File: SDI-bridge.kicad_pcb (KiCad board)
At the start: 4 copper layers, 68 x 32.6 mm, 168 parts, among them J1 031-70526-21, J2 WE_68715014522, J3 031-70526-21, J4 MC-HVT1-S04-G, J5 MC-HVT1-S04-G, U1 GS2971A, U2 MAX8902B, U3 GS2988, U4 CrossLink_LIF-MD6000-6JMG80I, U5 SC18IS602BIPW, Y1 ABM7_27.000MH_D2Y_T

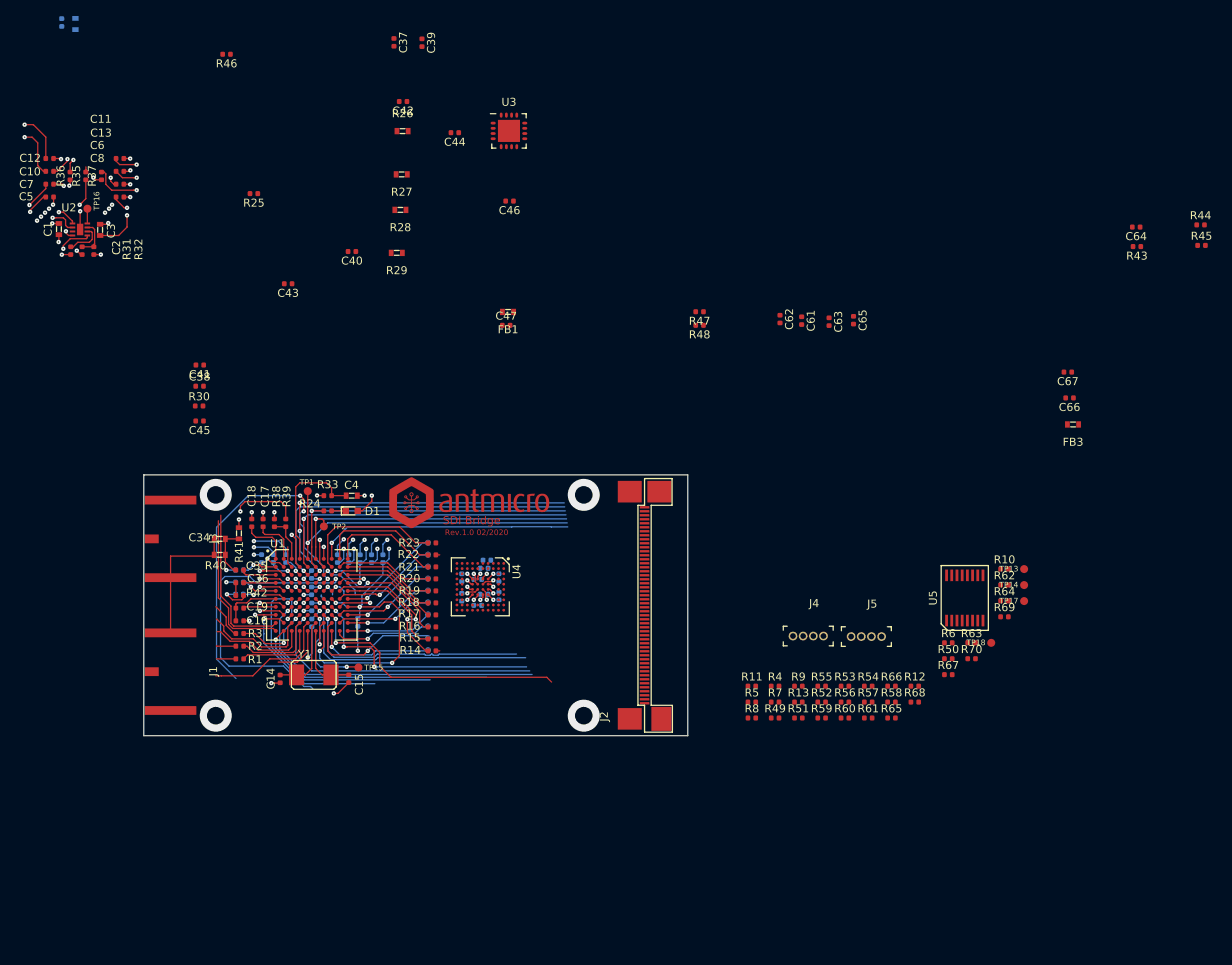
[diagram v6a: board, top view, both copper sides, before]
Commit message: Update component placement
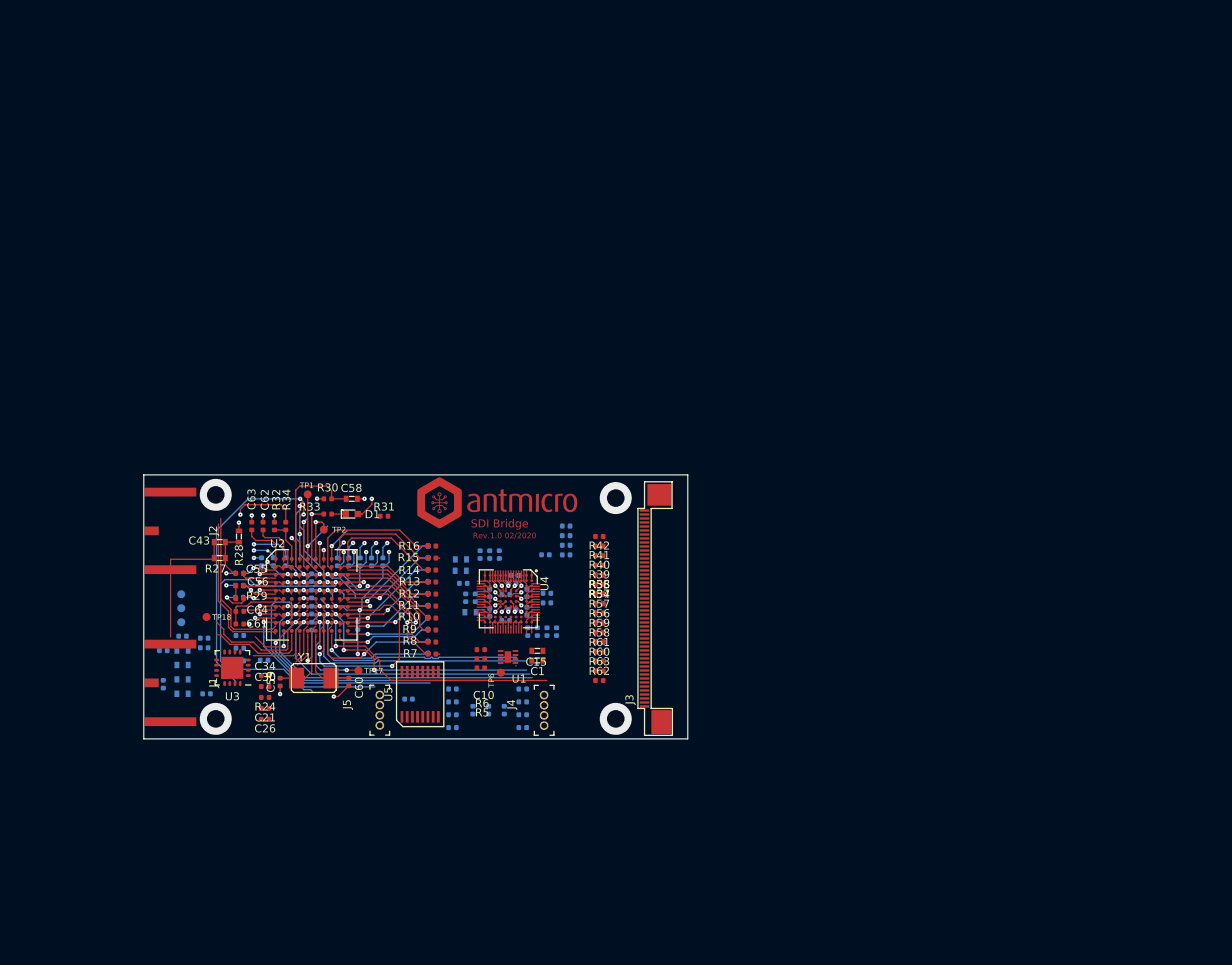
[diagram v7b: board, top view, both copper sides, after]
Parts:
- removed the C11 at (97.0, 60.5)
- removed the C12 at (88.2, 60.5)
- removed the C13 at (97.0, 62.1)
- removed the C2 at (90.9, 72.0)
- removed the C3 at (94.5, 69.4)
- removed the C38 at (107.0, 88.9)
- removed the C42 at (132.4, 53.3)
- removed the C43 at (118.0, 76.1)
- removed the C45 at (107.0, 93.3)
- removed the C48 at (139.8, 115.3)
- removed the C5 at (88.2, 65.3)
- removed the C51 at (141.7, 116.3)
- removed the C52 at (142.6, 111.7)
- removed the C58 at (142.9, 110.7)
- removed the C59 at (142.5, 114.9)
- removed the C6 at (97.0, 63.7)
- removed the C60 at (144.4, 115.1)
- removed the C61 at (182.2, 80.7)
- removed the C7 at (88.2, 63.7)
- removed the C8 at (97.0, 65.3)
- removed the J2 at (162.0, 116.3)
- removed the R10 at (207.6, 111.8)
- removed the R11 at (176.0, 126.4)
- removed the R12 at (196.4, 126.4)
- removed the R13 at (181.8, 128.4)
- removed the R30 at (106.9, 91.4)
- removed the R32 at (93.8, 72.0)
- removed the R35 at (92.8, 62.6)
- removed the R36 at (90.8, 62.6)
- removed the R4 at (178.9, 126.4)
- removed the R64 at (207.6, 115.8)
- removed the R68 at (196.4, 128.4)
- removed R69, R70: R_0R_0402, antmicro-footprints:0402-res
- removed the R8 at (176.0, 130.4)
- removed the R9 at (181.8, 126.4)
- removed the TP16 at (93.0, 66.7)
- removed the U2 at (92.0, 69.3)
- added C15: C_10u_0603, antmicro-footprints:0603-cap, F.Cu at (149.2, 122.0)
- added C19: C_10n_0402, antmicro-footprints:0402-cap, B.Cu at (138.6, 126.8)
- added C20: C_10n_0402, antmicro-footprints:0402-cap, B.Cu at (147.4, 128.4)
- added C21: C_10n_0402, antmicro-footprints:0402-cap, F.Cu at (115.2, 129.2)
- added C24: C_1u_0402, antmicro-footprints:0402-cap, B.Cu at (138.6, 128.4)
- added C25: C_1u_0402, antmicro-footprints:0402-cap, B.Cu at (147.4, 126.8)
- added C26: C_1u_0402, antmicro-footprints:0402-cap, F.Cu at (115.2, 130.6)
- added C27: C_5n6_0402, antmicro-footprints:0402-res, B.Cu at (104.8, 120.2)
- added C28: C_1u_0402, antmicro-footprints:0402-cap, B.Cu at (138.6, 130.0)
- added C29: C_1u_0402, antmicro-footprints:0402-cap, B.Cu at (147.4, 131.6)
- added C30: C_1u_0402, antmicro-footprints:0402-cap, F.Cu at (115.2, 126.5)
- added C32: C_10n_0402, antmicro-footprints:0402-cap, B.Cu at (138.6, 131.6)
- added C33: C_10n_0402, antmicro-footprints:0402-cap, B.Cu at (147.4, 130.0)
- added C34: C_10n_0402, antmicro-footprints:0402-cap, F.Cu at (115.2, 125.1)
- added C36: C_10n_0402, antmicro-footprints:0402-cap, B.Cu at (102.4, 126.2)
- added C39: C_100n_0402_6V3, antmicro-footprints:0402-cap, B.Cu at (148.0, 119.6)
- added C40: C_100n_0402_6V3, antmicro-footprints:0402-cap, B.Cu at (147.9, 114.8)
- added C44: C_100n_0402_6V3, antmicro-footprints:0402-cap, B.Cu at (146.4, 112.6)
- added C53: C_100n_0402_6V3, antmicro-footprints:0402-cap, B.Cu at (147.9, 117.0)
- added C54: C_100n_0402_6V3, antmicro-footprints:0402-cap, B.Cu at (145.2, 118.2)
- added J3: WE_68715014522_ONE-SIDE, antmicro-footprints:WE_68715014522_ONE-SIDE, F.Cu at (162.0, 116.7)
- added R21: R_0R_0402, antmicro-footprints:0402-res, B.Cu at (143.1, 129.4)
- added R22: R_0R_0402, antmicro-footprints:0402-res, B.Cu at (141.1, 129.4)
- added R23: R_0R_0402, antmicro-footprints:0402-res, B.Cu at (145.1, 129.4)
- added R24: R_0R_0402, antmicro-footprints:0402-res, F.Cu at (115.2, 127.8)
- added R38: R_0R_0402, antmicro-footprints:0402-res, F.Cu at (156.9, 112.5)
- added R39: R_0R_0402, antmicro-footprints:0402-res, F.Cu at (156.9, 111.3)
- added R40: R_0R_0402, antmicro-footprints:0402-res, F.Cu at (156.9, 110.1)
- added R41: R_0R_0402, antmicro-footprints:0402-res, F.Cu at (156.9, 108.9)
- added R42: R_0R_0402, antmicro-footprints:0402-res, F.Cu at (156.9, 107.7)
- added R44: R_0R_0402, antmicro-footprints:0402-res, B.Cu at (156.9, 113.7)
- added R45: R_0R_0402, antmicro-footprints:0402-res, B.Cu at (156.9, 112.5)
- added R6: R_120k_0402, antmicro-footprints:0402-res, F.Cu at (142.1, 123.0)
- added R66: R_2k37_0402, antmicro-footprints:0402-res, B.Cu at (152.8, 108.8)
- added TP6: TP_SMD1MM, antmicro-footprints:Testpoint_smd_1mm, F.Cu at (144.6, 124.7)
- added U1: MAX8902B, antmicro-footprints:TDFN2x2, F.Cu at (145.5, 122.8)
- C10: value C_1u_0402 -> C_10n_0402
- C18: renamed from C37; moved to B.Cu
- C22: renamed from C39; moved to B.Cu
- C23: renamed from C40; moved to B.Cu
- C31: renamed from C44; moved to B.Cu
- C37: renamed from C47; moved to B.Cu
- C41: value C_1u_0402 -> C_100n_0402_6V3; moved to B.Cu
- C42: renamed from C62; moved to B.Cu
- C45: renamed from C64; moved to B.Cu
- C46: value C_10n_0402 -> C_100n_0402_6V3; moved to B.Cu
- C47: renamed from C66; moved to B.Cu
- C48: renamed from C63; moved to B.Cu
- C51: renamed from C67; moved to B.Cu
- C52: renamed from C65; moved to B.Cu
- FB1, FB3, R1, R2, R3, R47, R49, R50, R51, R52, R53, R67: moved to B.Cu
- R17: renamed from R26; moved to B.Cu
- R18: renamed from R27; moved to B.Cu
- R19: renamed from R28; moved to B.Cu
- R20: renamed from R29; moved to B.Cu
- R26: renamed from R43; moved to B.Cu
- R31: value R_120k_0402 -> R_0R_0402
- R35: renamed from R44; moved to B.Cu
- R36: renamed from R45; moved to B.Cu
- R4: renamed from R25; moved to B.Cu
- R43: renamed from R6; moved to B.Cu
- R46, R48: value R_2k37_0402 -> R_0R_0402; moved to B.Cu
- R5: value R_2k37_0402 -> R_120k_0402
- R63: value R_2k37_0402 -> R_0R_0402
- R64: renamed from R7; moved to B.Cu
- R65: value R_0R_0402 -> R_2k37_0402; moved to B.Cu
- R68: renamed from R66; moved to B.Cu
- TP3: renamed from TP13; moved to B.Cu
- TP4: renamed from TP14; moved to B.Cu
- TP5: renamed from TP17; moved to B.Cu
- moved TP3 105.4 mm to (104.7, 115.0), turned to 180 degrees
- moved TP4 105.4 mm to (104.7, 116.7), turned to 180 degrees
- moved TP5 105.4 mm to (104.7, 118.5), turned to 180 degrees
- moved TP18 98.1 mm to (107.8, 117.7), turned to 180 degrees
- moved R36 97.0 mm to (143.2, 110.0), turned to 270 degrees
- moved R35 96.9 mm to (144.4, 110.0), turned to 270 degrees
- moved C45 86.7 mm to (150.4, 114.8)
- moved C38 86.2 mm to (139.9, 113.6), turned to 180 degrees
- moved R26 86.2 mm to (150.4, 116.0), turned to 0 degrees
- moved FB2 83.6 mm to (139.6, 112.0), turned to 0 degrees
- moved R46 83.0 mm to (156.9, 116.1)
- moved C1 80.5 mm to (149.2, 123.2), turned to 0 degrees
- moved R37 80.5 mm to (156.9, 113.7), turned to 180 degrees
- moved C10 80.5 mm to (142.1, 121.8)
- moved C47 79.5 mm to (140.2, 115.4), turned to 90 degrees
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- renumbered C28 to C11, C29 to C12, C30 to C13, C31 to C14, C32 to C16, C33 to C17, C20 to C2, C21 to C3, C9 to C35, C53 to C38, C22 to C4, C34 to C43, C23 to C5, C35 to C55, C36 to C56, C4 to C58, C14 to C59, C24 to C6, C15 to C60, C16 to C61, C17 to C62, C18 to C63, C19 to C64, C25 to C7, C26 to C8, C27 to C9, J3 to J2, R17 to R10, R18 to R11, R19 to R12, R20 to R13, R21 to R14, R22 to R15, R23 to R16, R34 to R25, R40 to R27, R41 to R28, R42 to R29, R33 to R30, R38 to R32, R24 to R33, R39 to R34, R14 to R7, R15 to R8, R16 to R9, TP6 to TP10, TP7 to TP11, TP8 to TP12, TP9 to TP13, TP10 to TP14, TP11 to TP15, TP12 to TP16, TP15 to TP17, TP3 to TP7, TP4 to TP8, TP5 to TP9, U1 to U2
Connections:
- net +VSW renamed IO_VDD
- net /VCO_VDD renamed VCO_VDD
- C10 pad 1: +3.3VA -> +1V2
- C10 pad 2: GNDA -> Net-(C10-Pad2)
- C18 pad 1: VDD -> CD_VDD
- C22 pad 1: VDD -> CD_VDD
- C38 pad 1: /VCCA_DPHY -> VCCA_DPHY
- C41 pad 1: +3V3 -> /VCCIO
- C46 pad 1: GNDA -> /VCCIO
- C46 pad 2: VDD -> GNDREF
- C49 pad 1: /VCCIO -> VCCA_DPHY
- C49 pad 2: GNDREF -> /GNDPLL_DPHY
- C57 pad 1: /VCCA_DPHY -> /VCCIO
- FB2 pad 2: /VCCA_DPHY -> VCCA_DPHY
- R31 pad 1: +1V2 -> /LOCKED
- R31 pad 2: Net-(R31-Pad2) -> /LOCKED_IN
- R35 pad 2: /VCCIO -> VCC_IO
- R36 pad 2: /VCCIO -> VCC_IO
- R37 pad 1: +1V2 -> /SDA1
- R37 pad 2: VPP -> /SDA_CL
- R46 pad 1: /SCL_GS -> /MIPI1_D0_N
- R46 pad 2: Net-(R4-Pad2) (its old number) -> /DPHY1_D0_N
- R47 pad 1: +3V3 -> /MIPI1_D0_P
- R47 pad 2: Net-(R4-Pad2) (its old number) -> /DPHY1_D0_P
- R48 pad 1: /SDA_GS -> /MIPI1_D1_N
- R48 pad 2: Net-(R4-Pad2) (its old number) -> /DPHY1_D1_N
- R49 pad 1: /DPHY0_D2_N -> /MIPI1_D1_P
- R49 pad 2: /MIPI0_D2_N -> /DPHY1_D1_P
- R5 pad 1: /SDA_CL -> +1V2
- R5 pad 2: Net-(R4-Pad2) (its old number) -> Net-(R5-Pad2)
- R50 pad 1: /DPHY0_D2_P -> /MIPI1_D2_N
- R50 pad 2: /MIPI0_D2_P -> /DPHY1_D2_N
- R51 pad 1: /DPHY0_D3_N -> /MIPI1_D2_P
- R51 pad 2: /MIPI0_D3_N -> /DPHY1_D2_P
- R52 pad 1: /DPHY0_D3_P -> /MIPI1_D3_N
- R52 pad 2: /MIPI0_D3_P -> /DPHY1_D3_N
- R53 pad 1: /DPHY1_CLK_N -> /MIPI1_D3_P
- R53 pad 2: /MIPI1_CLK_N -> /DPHY1_D3_P
- R54 pad 1: /DPHY1_CLK_P -> /DPHY0_CLK_N
- R54 pad 2: /MIPI1_CLK_P -> /MIPI0_CLK_N
- R55 pad 1: /DPHY1_D0_N -> /DPHY0_CLK_P
- R55 pad 2: /MIPI1_D0_N -> /MIPI0_CLK_P
- R56 pad 1: /DPHY1_D0_P -> /DPHY0_D0_N
- R56 pad 2: /MIPI1_D0_P -> /MIPI0_D0_N
- R57 pad 1: /DPHY1_D1_N -> /DPHY0_D0_P
- R57 pad 2: /MIPI1_D1_N -> /MIPI0_D0_P
- R58 pad 1: /DPHY1_D1_P -> /DPHY0_D1_N
- R58 pad 2: /MIPI1_D1_P -> /MIPI0_D1_N
- R59 pad 1: /DPHY1_D2_N -> /DPHY0_D1_P
- R59 pad 2: /MIPI1_D2_N -> /MIPI0_D1_P
- R60 pad 1: /DPHY1_D2_P -> /DPHY0_D2_N
- R60 pad 2: /MIPI1_D2_P -> /MIPI0_D2_N
- R61 pad 1: /DPHY1_D3_N -> /DPHY0_D2_P
- R61 pad 2: /MIPI1_D3_N -> /MIPI0_D2_P
- R62 pad 1: /DPHY1_D3_P -> /DPHY0_D3_N
- R62 pad 2: /MIPI1_D3_P -> /MIPI0_D3_N
- R63 pad 1: /SDA_CL -> /DPHY0_D3_P
- R63 pad 2: Net-(R63-Pad2) -> /MIPI0_D3_P
- R64 pad 1: /SCL_CL -> Net-(R64-Pad1)
- R64 pad 2: Net-(R63-Pad2) -> /SCL_CL
- R65 pad 1: +3V3 -> Net-(R64-Pad1)
- R65 pad 2: Net-(R63-Pad2) -> /SDA_CL
- R67 pad 1: /SDA_GS -> +3V3
- R67 pad 2: /SDA -> Net-(R64-Pad1)
- R68 pad 1: /SDA_GS -> Net-(R64-Pad1)
- R68 pad 2: Net-(R63-Pad2) -> /SDA_GS
- U3 pad 9: VDD -> CD_VDD
- U4 pad D1: Net-(U4-PadD1) -> /IOPROC_EN_~DIS~
- U4 pad D2: /VCCA_DPHY -> VCCA_DPHY
- U4 pad D4: /VCCA_DPHY -> VCCA_DPHY
- U4 pad D7: /VCCA_DPHY -> VCCA_DPHY
- U4 pad E2: /LOCKED -> /LOCKED_IN
- U4 pad E7: /VCCA_DPHY -> VCCA_DPHY
- U4 pad F4: /VCCIO -> VCC_IO
- U4 pad F5: /VCCIO -> VCC_IO
- U4 pad F6: /VCCIO -> VCC_IO
- U4 pad F7: /VCCIO -> VCC_IO
- U4 pad G4: /VCCIO -> VCC_IO
- U4 pad K2: Net-(U4-PadK2) -> /Audio_EN_~DIS~
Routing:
- net /Y_1ANC: track 42.4 -> 10.3 mm
- net /DATA_ERRORb: track 43.3 -> 11.6 mm
- net /LOCKED: track 40.4 -> 9.11 mm
- net /F_DE: track 39.2 -> 8.67 mm
- net /V_VSYNC: track 38.2 -> 8.96 mm
- net /H_HSYNC: track 41.9 -> 13.0 mm
- net /PCLK: track 32.3 -> 5.80 mm
- net +1V2: track 25.5 -> 9.68 mm, vias 13 -> 6
- net +3V3: track 16.9 -> 3.84 mm, vias 10 -> 2
- net +3.3VA: track 33.9 -> 21.2 mm, vias 7 -> 5
- net VPP: track 22.2 -> 10.1 mm, vias 7 -> 4
- net /AUDIO_OUTPUT_CH5_6: track 16.0 -> 5.12 mm
- net GNDREF: track 55.7 -> 46.5 mm, vias 36 -> 24
- net VCC_IO: track 0.00 -> 7.32 mm, vias 0 -> 5
- net GNDA: track 54.9 -> 48.1 mm, vias 30 -> 25
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- added copper zone on In1.Cu, net +VSW
- removed copper zone on In1.Cu, net IO_VDD
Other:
- board size 68 x 32.6 mm -> 68 x 33 mm

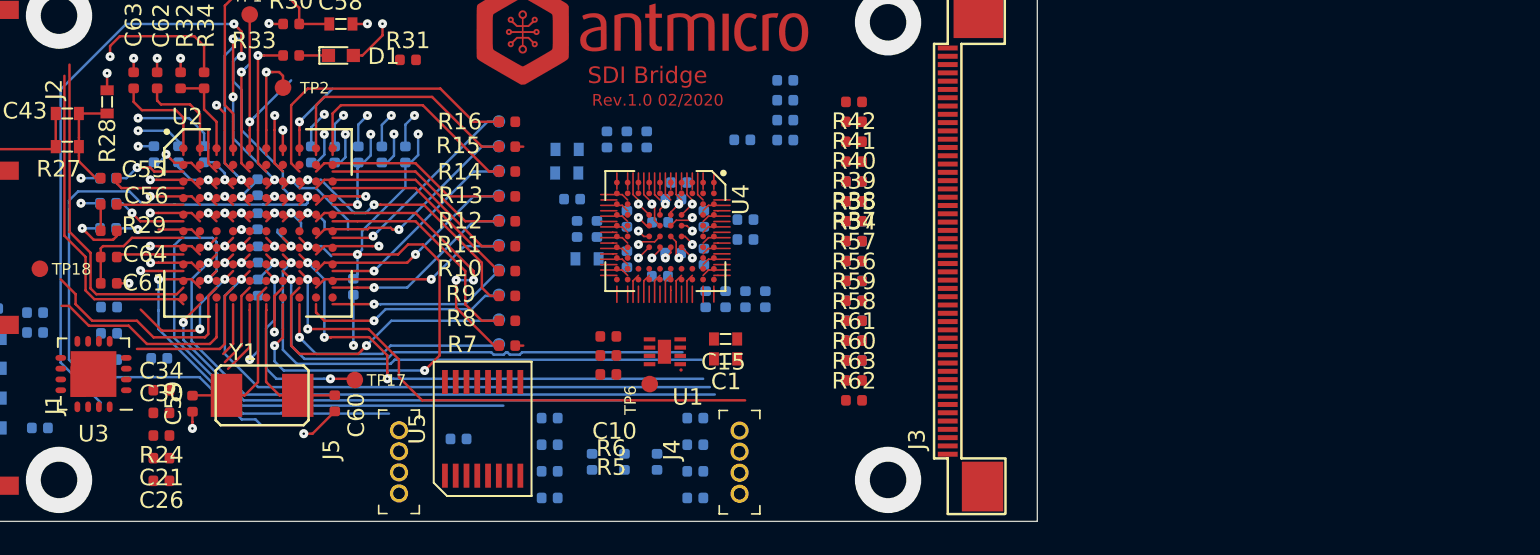
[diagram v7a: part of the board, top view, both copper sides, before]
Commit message: Schematic changes after design review
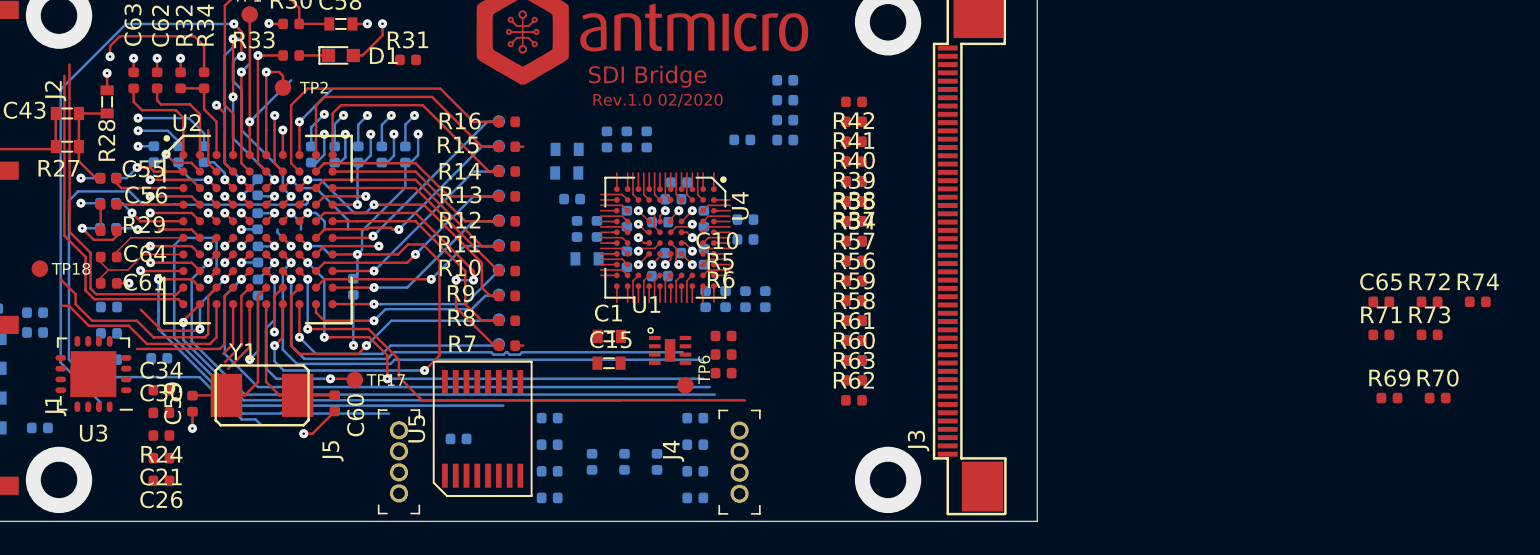
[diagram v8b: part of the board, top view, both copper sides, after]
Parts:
- added C65: C_10n_0402, antmicro-footprints:0402-cap, F.Cu at (188.8, 119.8)
- added R69: R_0R_0402, antmicro-footprints:0402-res, F.Cu at (189.2, 125.6)
- added R70: R_0R_0402, antmicro-footprints:0402-res, F.Cu at (192.2, 125.6)
- added R71: R_0R_0402, antmicro-footprints:0402-res, F.Cu at (188.8, 121.8)
- added R72: R_0R_0402, antmicro-footprints:0402-res, F.Cu at (191.7, 119.8)
- added R73: R_0R_0402, antmicro-footprints:0402-res, F.Cu at (191.7, 121.8)
- added R74: R_0R_0402, antmicro-footprints:0402-res, F.Cu at (194.6, 119.8)
- moved C15 7.18 mm to (142.2, 123.5), turned to 180 degrees
- moved C1 7.14 mm to (142.2, 121.8), turned to 180 degrees
- moved R5 7.05 mm to (149.1, 122.9), turned to 180 degrees
- moved R6 7.03 mm to (149.1, 124.1), turned to 0 degrees
- moved C10 6.95 mm to (149.1, 121.8), turned to 180 degrees
- moved TP6 2.26 mm to (146.8, 124.8), turned to 90 degrees
- moved U2 0.40 mm to (121.0, 115.4)
- moved U4 0.40 mm to (145.6, 115.9)
- moved U1 0.38 mm to (145.9, 122.6), turned to 0 degrees
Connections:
- C18 pad 1: CD_VDD -> VDD
- C22 pad 1: CD_VDD -> VDD
- C61 pad 1: /AGCP -> /AGCN
- C62 pad 2: /LF -> /VBG
- C63 pad 2: /VBG -> /LF
- C64 pad 1: /AGCN -> /AGCP
- C64 pad 2: /AGCP -> /AGCN
- R20 pad 1: GNDA -> GND
- U1 pad 3: Net-(U1-Pad3) -> +3V3
- U3 pad 9: CD_VDD -> VDD
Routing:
- net /AGCN: track 4.08 -> 6.88 mm
- net /AGCP: track 7.36 -> 4.68 mm
- net Net-(R35-Pad1): track 0.00 -> 1.76 mm
- net VCC_IO: track 7.32 -> 5.56 mm
- net VCCA_DPHY: track 6.15 -> 4.39 mm
- net GNDREF: track 46.5 -> 48.3 mm
